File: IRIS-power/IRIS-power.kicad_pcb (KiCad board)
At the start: 2 copper layers, 58.5 x 65 mm, 71 parts, among them J1 PCIE1X, J2 Powerpole, J3 PJ-047AH, Q1 IRLML6402TRPBF, U1 TPS2121, U2 LTC3110, U3 TPS565201, U4 TPS55340

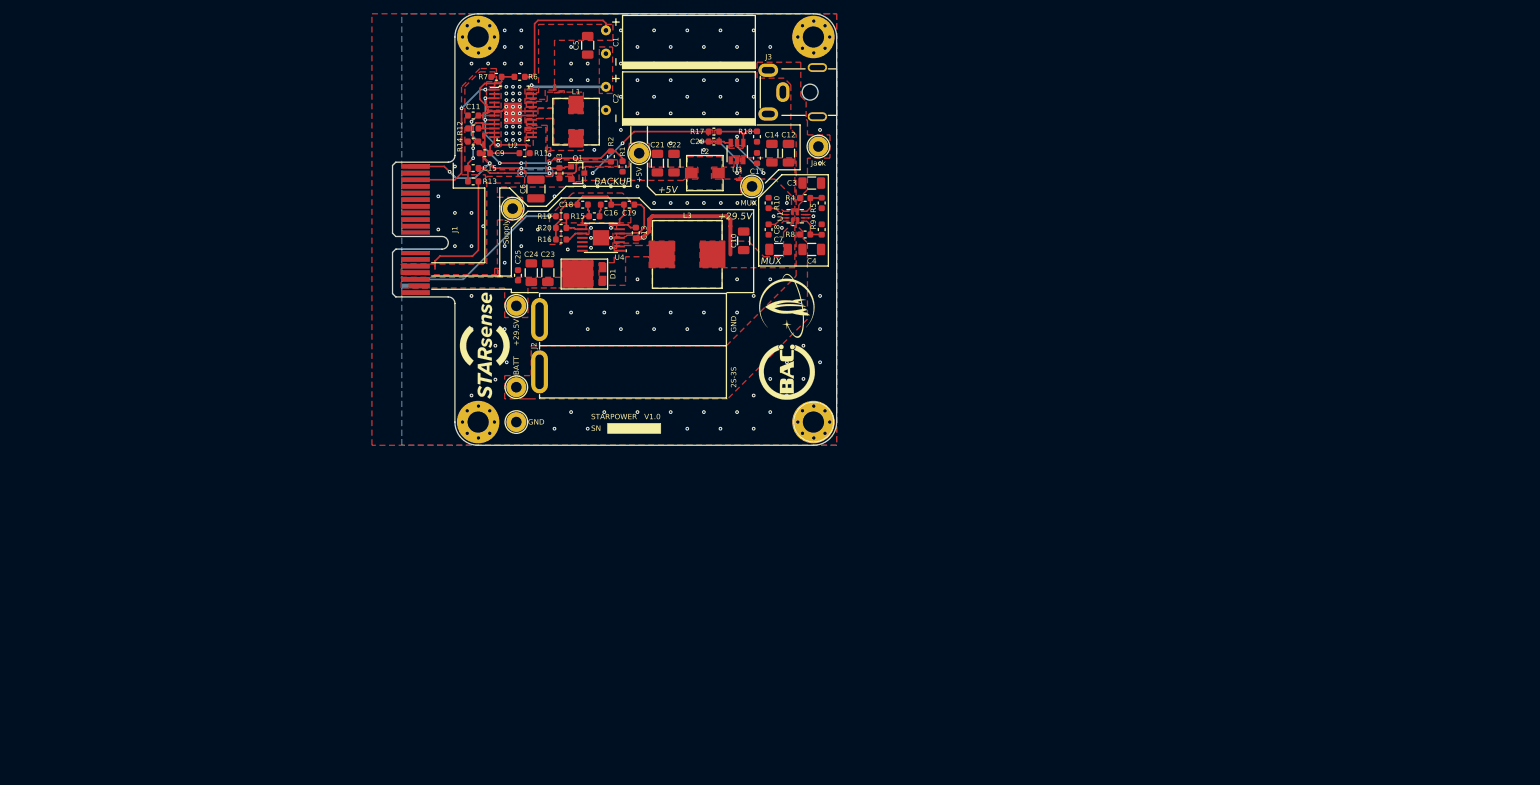
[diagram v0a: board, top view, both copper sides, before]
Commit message: Started layout
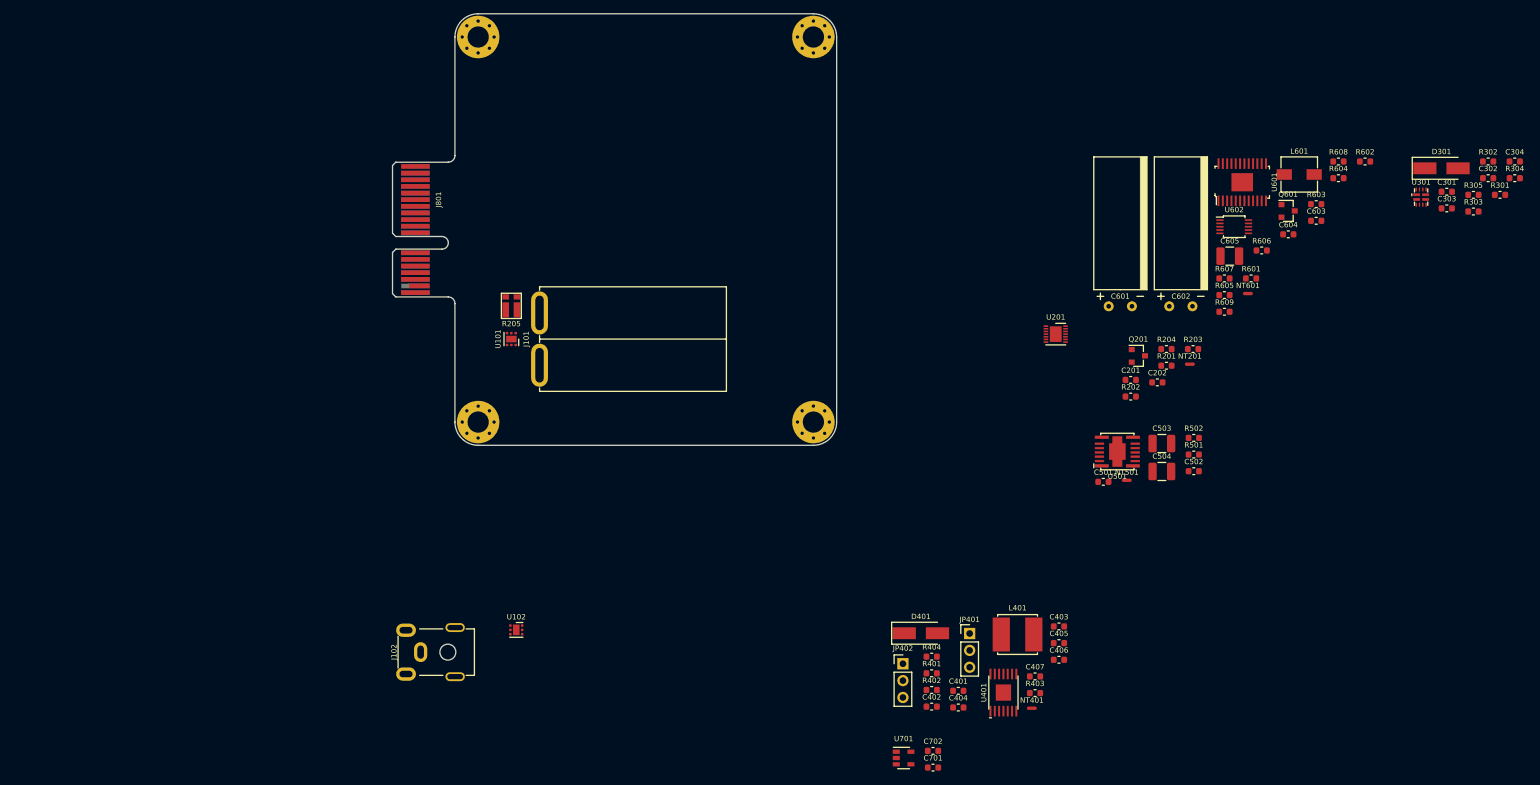
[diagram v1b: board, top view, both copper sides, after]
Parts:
- removed +29.5V, +5V, BATT, GND, Jack, MUX, Supply: TestPoint, TestPoint:TestPoint_Loop_D2.60mm_Drill1.6mm_Beaded
- removed C1, C2: 3.3F, STARpower:SCCR20B335PRB
- removed C10, C12, C14, C23, C24, C3, C4, C5, C7: 10uF, Capacitor_SMD:C_1206_3216Metric
- removed C11: 1nF, Capacitor_SMD:C_0603_1608Metric
- removed C13, C17, C20: 100nF, Capacitor_SMD:C_0603_1608Metric
- removed C15: 10pF, Capacitor_SMD:C_0603_1608Metric
- removed C16: 1.2nF, Capacitor_SMD:C_0603_1608Metric
- removed C18: 68nF, Capacitor_SMD:C_0603_1608Metric
- removed C19: 27nF, Capacitor_SMD:C_0603_1608Metric
- removed C21, C22: 22uF, Capacitor_SMD:C_1206_3216Metric
- removed C25: 680nF, Capacitor_SMD:C_0603_1608Metric
- removed C6: 150uF, Capacitor_SMD:C_1210_3225Metric
- removed C8: 1uF, Capacitor_SMD:C_0603_1608Metric
- removed C9: 220nF, Capacitor_SMD:C_0603_1608Metric
- removed D1: FSV1045V, STARpower:TO-227
- removed G***: LOGO, STAR_logos:star_9x8
- removed G***: LOGO, STAR_logos:bac_logo
- removed G***: LOGO, STAR_logos:starsense_medium
- removed H1, H2, H3, H4: MountingHole_Pad, MountingHole:MountingHole_3.2mm_M3_Pad_Via
- removed J1: PCIE1X, Connector_PCBEdge:BUS_PCIexpress_x1
- removed J2: Powerpole, STARpower:1336G1
- removed J3: PJ-047AH, STARpower:CUI_PJ-047AH
- removed L1: 1.5uH, STARpower:744314150
- removed L2: 3.3uH, STARpower:744316330
- removed L3: 10uH, STARpower:7443251000
- removed Q1: IRLML6402TRPBF, Package_TO_SOT_SMD:SOT-23
- removed R1: 7.5k, Resistor_SMD:R_0603_1608Metric
- removed R10: 21.5k, Resistor_SMD:R_0603_1608Metric
- removed R11: 51.1R, Resistor_SMD:R_0603_1608Metric
- removed R12: 6.04k, Resistor_SMD:R_0603_1608Metric
- removed R13: 976k, Resistor_SMD:R_0603_1608Metric
- removed R14: 133k, Resistor_SMD:R_0603_1608Metric
- removed R15: 2.26k, Resistor_SMD:R_0603_1608Metric
- removed R16: 38.3k, Resistor_SMD:R_0603_1608Metric
- removed R17: 54.9k, Resistor_SMD:R_0603_1608Metric
- removed R18, R20, R8, R9: 10k, Resistor_SMD:R_0603_1608Metric
- removed R19: 232k, Resistor_SMD:R_0603_1608Metric
- removed R2: 2.49k, Resistor_SMD:R_0603_1608Metric
- removed R3: 3.3k, Resistor_SMD:R_0603_1608Metric
- removed R4: 15k, Resistor_SMD:R_0603_1608Metric
- removed R5: 16k, Resistor_SMD:R_0603_1608Metric
- removed R6: 3320k, Resistor_SMD:R_0603_1608Metric
- removed R7: 1910k, Resistor_SMD:R_0603_1608Metric
- removed U1: TPS2121, STARpower:TPS2121
- removed U2: LTC3110, STARpower:TSSOP-24_W4.40mm_1EP
- removed U3: TPS565201, Package_TO_SOT_SMD:TSOT-23-6
- removed U4: TPS55340, STARpower:HTSSOP-14
- added C201: 0.1uF, Capacitor_SMD:C_0603_1608Metric, F.Cu at (101.8, 55.2)
- added C202: 0.47uF, Capacitor_SMD:C_0603_1608Metric, F.Cu at (105.8, 55.5)
- added C301: 10uF, Capacitor_SMD:C_0603_1608Metric, F.Cu at (149.4, 26.8)
- added C302: 10uF, Capacitor_SMD:C_0603_1608Metric, F.Cu at (155.6, 24.8)
- added C303: 10uF, Capacitor_SMD:C_0603_1608Metric, F.Cu at (149.4, 29.3)
- added C304: 1uF, Capacitor_SMD:C_0603_1608Metric, F.Cu at (159.6, 22.3)
- added C401: 10uF, Capacitor_SMD:C_0603_1608Metric, F.Cu at (75.8, 102.0)
- added C402: 0.1uF, Capacitor_SMD:C_0603_1608Metric, F.Cu at (71.8, 104.4)
- added C403: 68nF, Capacitor_SMD:C_0603_1608Metric, F.Cu at (91.0, 92.3)
- added C404: 1.2nF, Capacitor_SMD:C_0603_1608Metric, F.Cu at (75.8, 104.5)
- added C405: 27nF, Capacitor_SMD:C_0603_1608Metric, F.Cu at (91.0, 94.8)
- added C406: 10uF, Capacitor_SMD:C_0603_1608Metric, F.Cu at (91.0, 97.3)
- added C407: 0.47uF, Capacitor_SMD:C_0603_1608Metric, F.Cu at (87.4, 99.8)
- added C501: 10uF, Capacitor_SMD:C_0603_1608Metric, F.Cu at (97.7, 70.5)
- added C502: 10uF, Capacitor_SMD:C_0603_1608Metric, F.Cu at (111.3, 68.9)
- added C503: 47uF, Capacitor_SMD:C_1210_3225Metric, F.Cu at (106.5, 64.7)
- added C504: 47uF, Capacitor_SMD:C_1210_3225Metric, F.Cu at (106.5, 68.9)
- added C601: 3.3F, star-common-lib:SCCR20B335PRB, F.Cu at (100.2, 44.1)
- added C602: 3.3F, star-common-lib:SCCR20B335PRB, F.Cu at (109.4, 44.1)
- added C603: 10uF, Capacitor_SMD:C_0603_1608Metric, F.Cu at (129.7, 31.2)
- added C604: 0.1uF, Capacitor_SMD:C_0603_1608Metric, F.Cu at (125.5, 33.2)
- added C605: 47uF, Capacitor_SMD:C_1210_3225Metric, F.Cu at (116.7, 36.5)
- added C701: 1uF, Capacitor_SMD:C_0603_1608Metric, F.Cu at (72.0, 113.5)
- added C702: 10uF, Capacitor_SMD:C_0603_1608Metric, F.Cu at (72.0, 111.0)
- added D301: D_Schottky, Diode_SMD:D_SMA_Handsoldering, F.Cu at (148.6, 23.3)
- added D401: D_Schottky, Diode_SMD:D_SMA_Handsoldering, F.Cu at (70.2, 93.3)
- added J101: Powerpole, star-common-lib:Powerpole_1336G1, F.Cu at (12.8, 49.0)
- added J102: PJ-047AH, star-common-lib:CUI_PJ-047AH, F.Cu at (-2.81, 96.2)
- added J801: IRIS_physical, star-common-lib:IRIS_Physical, F.Cu at (0.00, 0.00)
- added JP401: Jumper_3_Bridged12, Connector_PinHeader_2.54mm:PinHeader_1x03_P2.54mm_Vertical, F.Cu at (77.5, 93.4)
- added JP402: Jumper_3_Bridged12, Connector_PinHeader_2.54mm:PinHeader_1x03_P2.54mm_Vertical, F.Cu at (67.5, 97.9)
- added L401: 8.2uH, star-common-lib:VLS6045AF, F.Cu at (84.8, 93.5)
- added L601: 1.5uH, star-common-lib:744316150, F.Cu at (127.2, 24.2)
- added NT201: Net-Tie_2, NetTie:NetTie-2_SMD_Pad0.5mm, F.Cu at (110.7, 52.8)
- added NT401: Net-Tie_2, NetTie:NetTie-2_SMD_Pad0.5mm, F.Cu at (86.9, 104.6)
- added NT501: Net-Tie_2, NetTie:NetTie-2_SMD_Pad0.5mm, F.Cu at (101.2, 70.3)
- added NT601: Net-Tie_2, NetTie:NetTie-2_SMD_Pad0.5mm, F.Cu at (119.4, 42.1)
- added Q201: 2N7002, Package_TO_SOT_SMD:SOT-23, F.Cu at (102.9, 51.5)
- added Q601: IRLML6402, Package_TO_SOT_SMD:SOT-23, F.Cu at (125.5, 29.7)
- added R201: 499k, Resistor_SMD:R_0603_1608Metric, F.Cu at (107.2, 53.0)
- added R202: 301k, Resistor_SMD:R_0603_1608Metric, F.Cu at (101.8, 57.7)
- added R203: 200k, Resistor_SMD:R_0603_1608Metric, F.Cu at (111.2, 50.5)
- added R204: 10k, Resistor_SMD:R_0603_1608Metric, F.Cu at (107.2, 50.5)
- added R205: 2m, star-common-lib:CST0612-FC-R002E, F.Cu at (8.50, 44.0)
- added R301: 2.49k, Resistor_SMD:R_0603_1608Metric, F.Cu at (157.4, 27.3)
- added R302: 1k, Resistor_SMD:R_0603_1608Metric, F.Cu at (155.6, 22.3)
- added R303: 10k, Resistor_SMD:R_0603_1608Metric, F.Cu at (153.4, 29.8)
- added R304: 2.49k, Resistor_SMD:R_0603_1608Metric, F.Cu at (159.6, 24.8)
- added R305: 38.3k, Resistor_SMD:R_0603_1608Metric, F.Cu at (153.4, 27.3)
- added R401: 2.49k, Resistor_SMD:R_0603_1608Metric, F.Cu at (71.8, 99.3)
- added R402: 38.3k, Resistor_SMD:R_0603_1608Metric, F.Cu at (71.8, 101.9)
- added R403: 232k, Resistor_SMD:R_0603_1608Metric, F.Cu at (87.4, 102.3)
- added R404: 10k, Resistor_SMD:R_0603_1608Metric, F.Cu at (71.8, 96.8)
- added R501: 10k, Resistor_SMD:R_0603_1608Metric, F.Cu at (111.3, 66.4)
- added R502: 2.49k, Resistor_SMD:R_0603_1608Metric, F.Cu at (111.3, 63.9)
- added R601: 10k, Resistor_SMD:R_0603_1608Metric, F.Cu at (119.9, 39.9)
- added R602: 3k, Resistor_SMD:R_0603_1608Metric, F.Cu at (137.1, 22.3)
- added R603: 10k, Resistor_SMD:R_0603_1608Metric, F.Cu at (129.7, 28.7)
- added R604: 3570k, Resistor_SMD:R_0603_1608Metric, F.Cu at (133.1, 24.8)
- added R605: 1150k, Resistor_SMD:R_0603_1608Metric, F.Cu at (115.9, 42.4)
- added R606: 3k, Resistor_SMD:R_0603_1608Metric, F.Cu at (121.5, 35.7)
- added R607: 1.1M, Resistor_SMD:R_0603_1608Metric, F.Cu at (115.9, 39.9)
- added R608: 150k, Resistor_SMD:R_0603_1608Metric, F.Cu at (133.1, 22.3)
- added R609: 10k, Resistor_SMD:R_0603_1608Metric, F.Cu at (115.9, 44.9)
- added U101: TVS1400DRV, Package_SON:WSON-6-1EP_2x2mm_P0.65mm_EP1x1.6mm, F.Cu at (8.50, 49.0)
- added U102: TVS1400DRV, Package_SON:WSON-6-1EP_2x2mm_P0.65mm_EP1x1.6mm, F.Cu at (9.25, 92.8)
- added U201: MAX17261, Package_DFN_QFN:DFN-14-1EP_3x3mm_P0.4mm_EP1.78x2.35mm, F.Cu at (90.5, 48.2)
- added U301: TPS2121, star-common-lib:TPS2121, F.Cu at (145.5, 27.6)
- added U401: TPS55340, star-common-lib:TPS55340, F.Cu at (82.6, 102.2)
- added U501: TPSM53604, star-common-lib:TPSM53604, F.Cu at (99.8, 65.9)
- added U601: LTC3110, star-common-lib:LTC3110, F.Cu at (118.6, 25.4)
- added U602: PCA9537, Package_SO:TSSOP-10_3x3mm_P0.5mm, F.Cu at (117.4, 32.1)
- added U701: TLV75733PDBV, Package_TO_SOT_SMD:SOT-23-5, F.Cu at (67.6, 112.1)
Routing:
- net GND: track 58.0 -> 0.00 mm, vias 157 -> 0
- net VDD: track 34.8 -> 0.00 mm, vias 3 -> 0
- net /PWR_STAT: track 32.7 -> 0.00 mm, vias 4 -> 0
- net /DIR: track 32.0 -> 0.00 mm, vias 4 -> 0
- net +MUX: track 30.2 -> 0.00 mm, vias 2 -> 0
- net +29.5V: track 25.1 -> 0.00 mm, vias 1 -> 0
- net /CAP_STAT: track 23.2 -> 0.00 mm, vias 2 -> 0
- net /Vcap: track 21.4 -> 0.00 mm
- net +5V: track 20.1 -> 0.00 mm, vias 2 -> 0
- net /FB: track 13.0 -> 0.00 mm, vias 2 -> 0
- net /Vmid: track 12.0 -> 0.00 mm, vias 1 -> 0
- net /FBVcap: track 10.7 -> 0.00 mm
- net Net-(C20-Pad1): track 9.85 -> 0.00 mm, vias 2 -> 0
- net /SS: track 8.72 -> 0.00 mm
- net Net-(R17-Pad2): track 7.70 -> 0.00 mm
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- removed copper zone on F.Cu, net +29.5V
- removed copper zone on F.Cu, net +5V
- removed copper zone on F.Cu, net +BATT
- removed copper zone on F.Cu, net +MUX
- removed copper zone on F.Cu, net /Vcap
- removed copper zone on F.Cu, net /Vmid
- removed copper zone on B.Cu, net GND
- removed copper zone on F.Cu, net GND
- removed copper zone on F.Cu, net Net-(C20-Pad1)
- removed copper zone on F.Cu, net Net-(D1-Pad2)
- removed copper zone on F.Cu, net Net-(L1-Pad1)
- removed copper zone on F.Cu, net Net-(L1-Pad2)
- removed copper zone on F.Cu, net VDC
- removed copper zone on F.Cu, net VDD
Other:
- board size 58.5 x 65 mm -> 66.9 x 65 mm
- net class Default: clearance 0.2 -> 0.25
- net class Low Clearance removed
- rule trace_clearance: 0.2 -> 0.25
- rule trace_min: 0.2 -> 0.25
- rule via_min_drill: 0.254 -> 0.25
- rule via_min_size: 0.508 -> 0.5588
- board text removed: "+29.5V"
- board text removed: "+5V"
- board text removed: "2S-3S"
- board text removed: "BACKUP"
- board text removed: "GND"
- board text removed: "MUX"
- board text removed: "SN"
- board text removed: "STARPOWER"
- board text removed: "V1.0"

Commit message: Updated layout
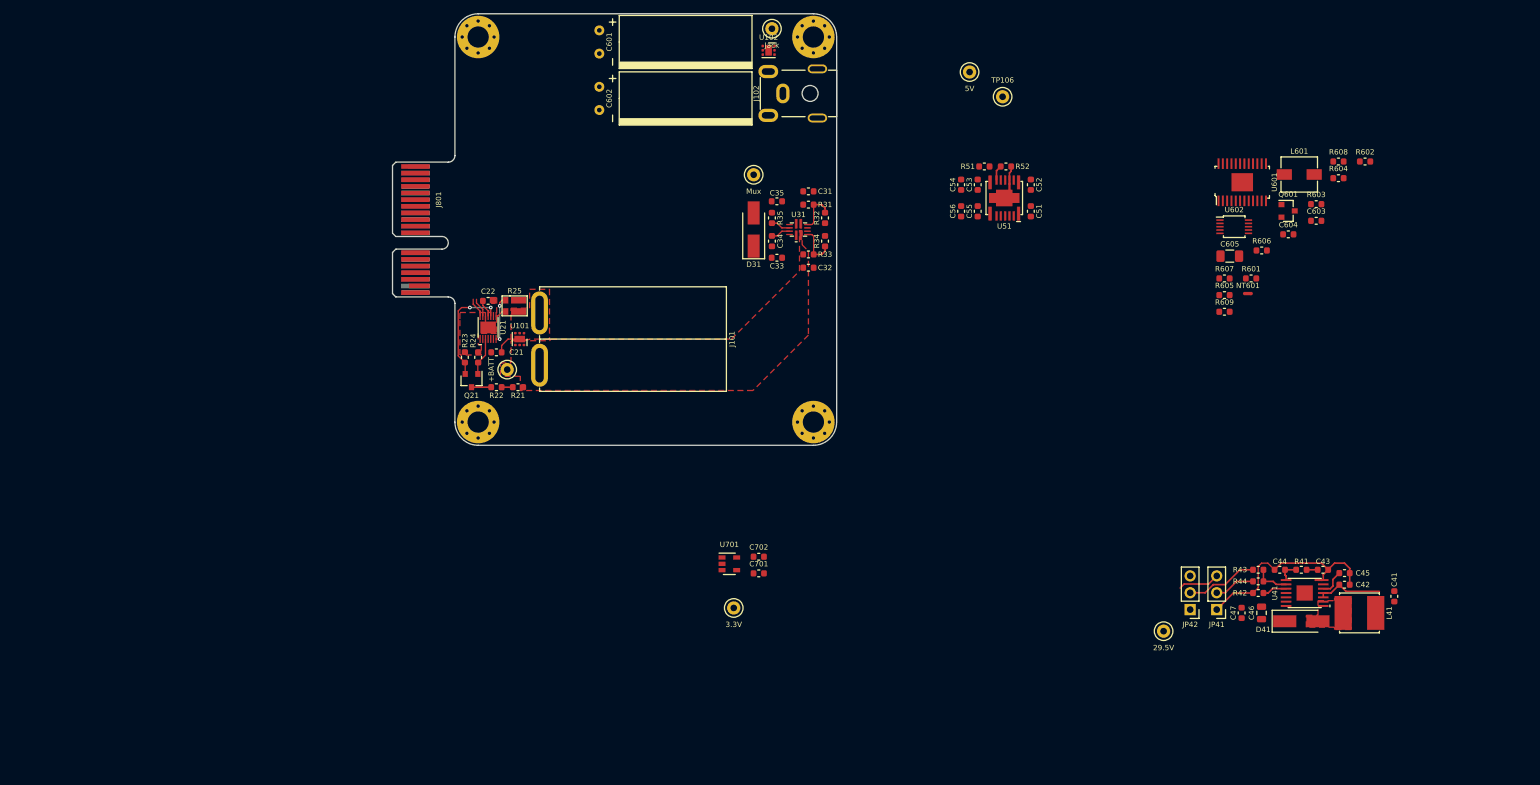
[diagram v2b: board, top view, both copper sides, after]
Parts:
- removed C201, C402: 0.1uF, Capacitor_SMD:C_0603_1608Metric
- removed C202: 0.47uF, Capacitor_SMD:C_0603_1608Metric
- removed C301, C302, C406: 10uF, Capacitor_SMD:C_0603_1608Metric
- removed C304: 1uF, Capacitor_SMD:C_0603_1608Metric
- removed C405: 27nF, Capacitor_SMD:C_0603_1608Metric
- removed C503, C504: 47uF, Capacitor_SMD:C_1210_3225Metric
- removed JP401: Jumper_3_Bridged12, Connector_PinHeader_2.54mm:PinHeader_1x03_P2.54mm_Vertical
- removed NT201, NT401: Net-Tie_2, NetTie:NetTie-2_SMD_Pad0.5mm
- removed Q201: 2N7002, Package_TO_SOT_SMD:SOT-23
- removed R205: 2m, star-common-lib:CST0612-FC-R002E
- removed R301, R304: 2.49k, Resistor_SMD:R_0603_1608Metric
- removed R302: 1k, Resistor_SMD:R_0603_1608Metric
- removed R303, R404: 10k, Resistor_SMD:R_0603_1608Metric
- removed R305: 38.3k, Resistor_SMD:R_0603_1608Metric
- removed U201: MAX17261, Package_DFN_QFN:DFN-14-1EP_3x3mm_P0.4mm_EP1.78x2.35mm
- removed U301: TPS2121, star-common-lib:TPS2121
- added C21: 0.1uF, Capacitor_SMD:C_0603_1608Metric, F.Cu at (6.25, 51.0)
- added C22: 0.47uF, Capacitor_SMD:C_0603_1608Metric, F.Cu at (5.00, 43.2)
- added C31: 10uF, Capacitor_SMD:C_0603_1608Metric, F.Cu at (53.2, 26.8)
- added C32: 10uF, Capacitor_SMD:C_0603_1608Metric, F.Cu at (53.2, 38.2)
- added C34: 1uF, Capacitor_SMD:C_0603_1608Metric, F.Cu at (47.8, 34.2)
- added C35: 10uF, Capacitor_SMD:C_0603_1608Metric, F.Cu at (48.5, 28.2)
- added C42: 0.1uF, Capacitor_SMD:C_0603_1608Metric, F.Cu at (134.0, 86.0)
- added C45: 27nF, Capacitor_SMD:C_0603_1608Metric, F.Cu at (134.0, 84.2)
- added C46: 10uF, Capacitor_SMD:C_0805_2012Metric, F.Cu at (121.5, 90.2)
- added C53: 10uF, Capacitor_SMD:C_0603_1608Metric, F.Cu at (78.8, 25.8)
- added C54: 10uF, Capacitor_SMD:C_0603_1608Metric, F.Cu at (76.2, 25.8)
- added C55: 10uF, Capacitor_SMD:C_0603_1608Metric, F.Cu at (78.8, 29.8)
- added C56: 10uF, Capacitor_SMD:C_0603_1608Metric, F.Cu at (76.2, 29.8)
- added JP41: Jumper_3_Bridged12, Connector_PinHeader_2.54mm:PinHeader_1x03_P2.54mm_Vertical, F.Cu at (114.8, 89.8)
- added NT41: Net-Tie_2, NetTie:NetTie-2_SMD_Pad0.5mm, F.Cu at (130.1, 85.3)
- added Q21: 2N7002, Package_TO_SOT_SMD:SOT-23, F.Cu at (2.50, 55.2)
- added R25: 2m, star-common-lib:CST0612-FC-R002E, F.Cu at (9.00, 44.0)
- added R31: 2.49k, Resistor_SMD:R_0603_1608Metric, F.Cu at (53.2, 28.8)
- added R32: 1k, Resistor_SMD:R_0603_1608Metric, F.Cu at (55.8, 30.8)
- added R33: 10k, Resistor_SMD:R_0603_1608Metric, F.Cu at (53.2, 36.2)
- added R34: 2.49k, Resistor_SMD:R_0603_1608Metric, F.Cu at (55.8, 34.2)
- added R35: 38.3k, Resistor_SMD:R_0603_1608Metric, F.Cu at (47.8, 30.8)
- added R44: 10k, Resistor_SMD:R_0603_1608Metric, F.Cu at (121.0, 85.5)
- added TP101: Jack, TestPoint:TestPoint_Keystone_5000-5004_Miniature, F.Cu at (47.8, 2.25)
- added TP102: Mux, TestPoint:TestPoint_Keystone_5000-5004_Miniature, F.Cu at (45.0, 24.2)
- added TP103: +BATT, TestPoint:TestPoint_Keystone_5000-5004_Miniature, F.Cu at (7.88, 53.6)
- added TP104: 5V, TestPoint:TestPoint_Keystone_5000-5004_Miniature, F.Cu at (77.5, 8.78)
- added TP105: 29.5V, TestPoint:TestPoint_Keystone_5000-5004_Miniature, F.Cu at (106.8, 93.0)
- added TP106: Backup, TestPoint:TestPoint_Keystone_5000-5004_Miniature, F.Cu at (82.5, 12.5)
- added TP107: 3.3V, TestPoint:TestPoint_Keystone_5000-5004_Miniature, F.Cu at (42.0, 89.5)
- added U21: MAX17261, star-common-lib:MAX17261, F.Cu at (5.00, 47.2)
- added U31: TPS2121, star-common-lib:TPS2121, F.Cu at (51.8, 32.5)
- C605: footprint Capacitor_SMD:C_1210_3225Metric -> Capacitor_SMD:C_1206_3216Metric
- moved R23 109.7 mm to (1.50, 51.8), turned to 90 degrees
- moved D31 104.0 mm to (45.0, 32.5), turned to 90 degrees
- moved R24 103.7 mm to (3.50, 51.8), turned to 90 degrees
- moved C33 101.2 mm to (48.5, 36.8), turned to 180 degrees
- moved J102 100.3 mm to (51.8, 12.0)
- moved R21 97.7 mm to (9.50, 56.2), turned to 180 degrees
- moved R22 95.6 mm to (6.25, 56.2), turned to 180 degrees
- moved U102 95.2 mm to (47.2, 5.50)
- moved C602 93.0 mm to (21.8, 12.8), turned to 270 degrees
- moved C601 88.0 mm to (21.8, 4.25), turned to 270 degrees
- moved C41 67.2 mm to (141.5, 87.8), turned to 90 degrees
- moved R41 57.8 mm to (127.5, 83.8)
- moved D41 57.3 mm to (127.5, 91.5)
- moved R51 53.6 mm to (79.8, 23.0)
- moved C44 52.7 mm to (124.2, 83.8), turned to 180 degrees
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- renumbered C303 to C33, C401 to C41, C403 to C43, C404 to C44, C407 to C47, C501 to C51, C502 to C52, D301 to D31, D401 to D41, JP402 to JP42, L401 to L41, NT501 to NT51, R201 to R21, R202 to R22, R203 to R23, R204 to R24, R401 to R41, R402 to R42, R403 to R43, R501 to R51, R502 to R52, U401 to U41, U501 to U51
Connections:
- net Net-(D401-Pad2) renamed /HV Supply/SW
- net Net-(NT501-Pad2) renamed /5V Supply/AGND
- net Net-(R403-Pad2) renamed /HV Supply/FB
- net Net-(R501-Pad2) renamed /5V Supply/FB
- C43 pad 2: GND -> /HV Supply/AGND
- C44 pad 2: GND -> /HV Supply/AGND
- D31 pad 2: Net-(C301-Pad2) -> /Power Mux/GND_P
- J801 pad B15: /Edge Connector/+29.5V -> /Edge Connector/FB_HV_N
- J801 pad B16: /Edge Connector/FB_HV_N -> /Edge Connector/+29.5V
- R24 pad 1: Net-(Q201-Pad1) -> /Fuel Gauge/SW
- R42 pad 1: GND -> /HV Supply/AGND
- U41 pad 7: Net-(JP401-Pad1) -> /HV Supply/AGND
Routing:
- net /HV Supply/AGND: track 0.00 -> 31.1 mm
- net /Fuel Gauge/CELLX: track 0.00 -> 16.3 mm, vias 0 -> 2
- net Net-(JP42-Pad2): track 0.00 -> 10.9 mm
- net /5V Supply/+MUX: track 0.00 -> 10.0 mm
- net /Fuel Gauge/CSN: track 0.00 -> 7.11 mm, vias 0 -> 2
- net /Power Mux/PRI: track 0.00 -> 6.40 mm
- net /Power Mux/CP2: track 0.00 -> 6.40 mm
- net /Edge Connector/FB_HV_N: track 0.00 -> 6.26 mm
- net Net-(JP41-Pad2): track 0.00 -> 6.17 mm
- net /Fuel Gauge/SW: track 0.00 -> 5.75 mm
- net /HV Supply/FB: track 0.00 -> 5.35 mm
- net /Fuel Gauge/-BATT: track 0.00 -> 4.15 mm
- net /HV Supply/SS: track 0.00 -> 3.96 mm
- net /HV Supply/FREQ: track 0.00 -> 3.68 mm
- net GND1: track 0.00 -> 3.62 mm
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- added copper zone on F.Cu, net /Fuel Gauge/+BATT
- added copper zone on F.Cu, net /Fuel Gauge/-BATT
- added copper zone on F.Cu, net /HV Supply/SW
- added copper zone on F.Cu, net GND1
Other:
- net class Low Clearance added: clearance 0.2, trace_width 0.2, via_dia 0.5588, via_drill 0.254
- rule trace_min: 0.25 -> 0.1524
- rule via_min_drill: 0.25 -> 0.2
